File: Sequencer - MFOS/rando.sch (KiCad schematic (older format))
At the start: 0 parts

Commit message: finished sequencer schematic
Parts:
- added 10k1, 4M7: R_US, symbol Device:R_US
- added C15, C20: 0.01u, symbol Device:C
- added C16, C17: 10u, symbol Device:CP1
- added C18, C19: 0.1u, symbol Device:C
- added C21: 0.001u, symbol Device:C
- added C24: 100p, symbol Device:C
- added D48: D, symbol Device:D
- added J73: +12V_Conn, symbol Connector:Conn_01x02_Female
- added J74: GND_Conn, symbol Connector:Conn_01x02_Female
- added J75: -12V_Conn, symbol Connector:Conn_01x02_Female
- added Q1: 2N3904, Package_TO_SOT_THT:TO-92_Inline, symbol Transistor_BJT:2N3904
- added R30, R31: 2M, symbol Device:R_US
- added R32, R35: 4k7, symbol Device:R_US
- added R33: 100K, symbol Device:R_US
- added R34, R36: 1M, symbol Device:R_US
- added U12: CD4094, symbol modular_synth:CD4094
- added U6: 40106, symbol 4xxx:40106
- added U8: TL082, symbol Amplifier_Operational:TL082
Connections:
- new net: C15.2, Q1.1 (E), R31.2
- new net: C15.1, R30.1, U8.3 (+)
- new net: 4M7.1, R33.2, R34.2, U8.1
- new net: 4M7.2, R32.1, U8.2 (-)
- new net: R33.1, U8.5 (+)
- new net: C20.2, R34.1, U8.6 (-)
- new net: D48.2 (A), U8.7
- new net: D48.1 (K), R35.1, U6.1
- new net: U12.2 (DATA), U6.2
- new net: C21.2, R36.2, U6.3
- new net: R36.1, U12.3 (CLK), U6.4
- new net: C24.1, U6.12
- new net: 10k1.1, C24.2, U12.1 (STB)
- new net +12V: C16.1, C18.1, C19.1, J73.1 (Pin_1), J73.2 (Pin_2), R31.1, U12.15 (ENA), U12.16 (VDD), U6.14 (VDD), U8.8 (V+)
- new net -12V: C17.2, J75.1 (Pin_1), J75.2 (Pin_2), Q1.2 (B), U8.4 (V-)
- new net CLK: U6.13
- new net DA: U12.4 (Q1)
- new net DB: U12.5 (Q2)
- new net DC: U12.6 (Q3)
- new net DD: U12.7 (Q4)
- new net Earth: 10k1.2, C16.2, C17.1, C18.2, C19.2, C20.1, C21.1, J74.1 (Pin_1), J74.2 (Pin_2), R30.2, R32.2, R35.2, U12.8 (VSS), U6.7 (VSS)
- no-connect marks 0 -> 7

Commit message: checked over sequencer schematic
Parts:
- R?: renamed from 10k1; value R_US -> 10K
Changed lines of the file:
@@
 $EndComp
 $Comp
-L Device:R_US 10k1
+L Device:R_US R?
 U 1 1 609B0E8A
 P 6150 3050
-F 0 "10k1" H 6218 3096 50  0000 L CNN
-F 1 "R_US" H 6218 3005 50  0000 L CNN
+F 0 "R?" H 6218 3096 50  0000 L CNN
+F 1 "10K" H 6218 3005 50  0000 L CNN
 F 2 "" V 6190 3040 50  0001 C CNN
 F 3 "~" H 6150 3050 50  0001 C CNN

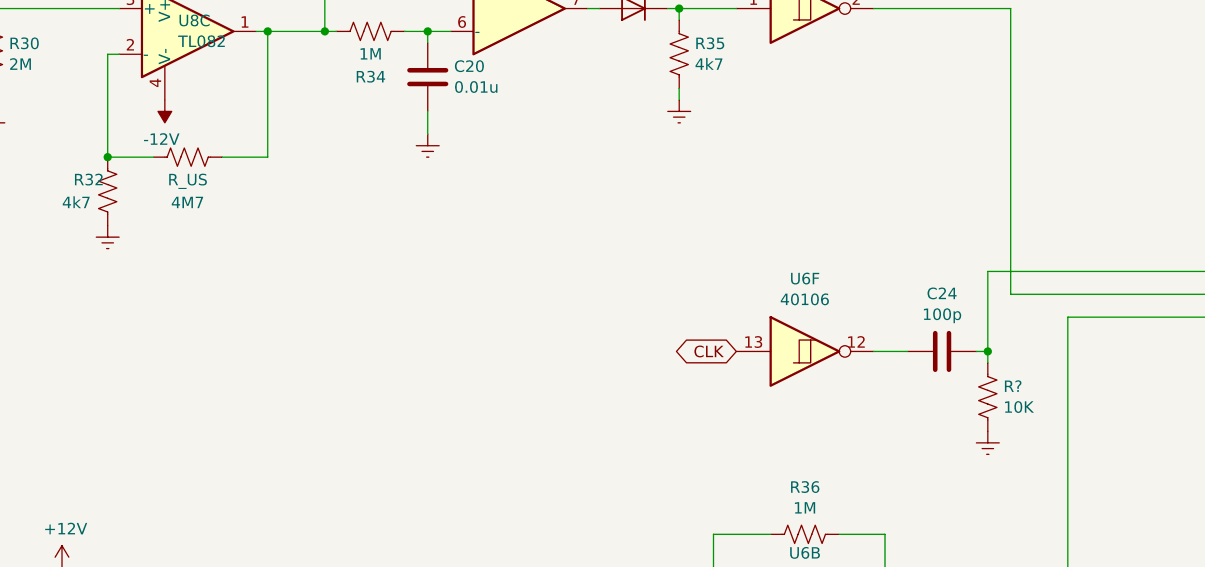
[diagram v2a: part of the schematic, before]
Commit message: sequencer pcb designed and base silkscreen
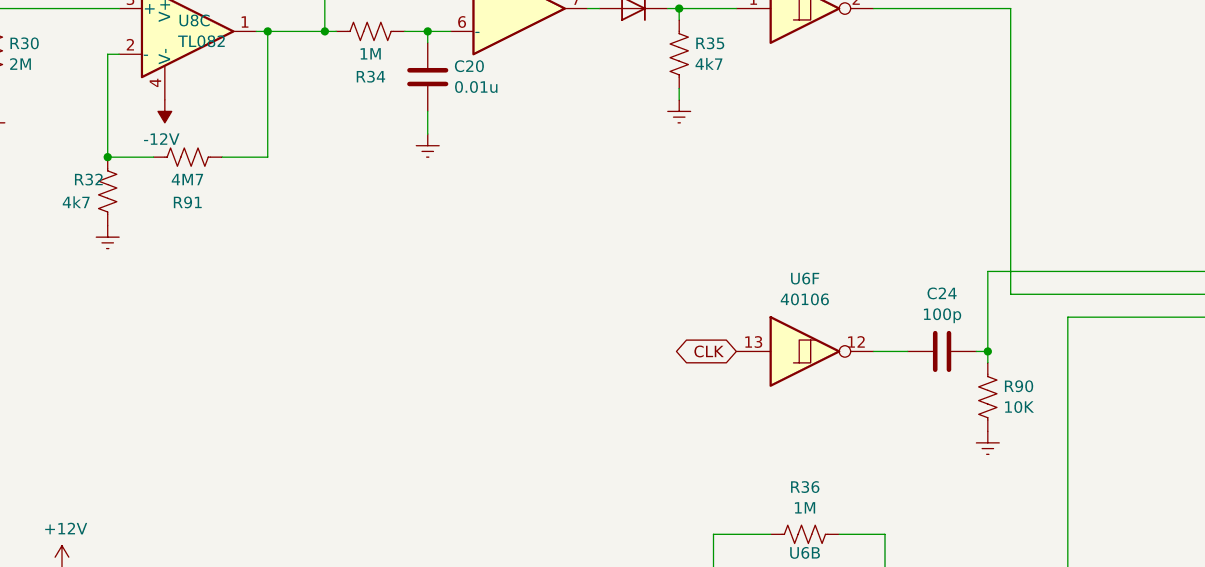
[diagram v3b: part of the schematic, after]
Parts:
- C15, C16, C17, C18, C19, C20, C21, C24: footprint (none) -> Capacitor_THT:C_Rect_L7.0mm_W2.5mm_P5.00mm
- D48: footprint (none) -> Diode_THT:D_T-1_P5.08mm_Horizontal
- J73, J74, J75: footprint (none) -> Connector_Wire:SolderWirePad_1x02_P3.81mm_Drill1mm
- R30, R31, R32, R33, R34, R35, R36: footprint (none) -> Resistor_THT:R_Axial_DIN0207_L6.3mm_D2.5mm_P7.62mm_Horizontal
- R90: renamed from R?; footprint (none) -> Resistor_THT:R_Axial_DIN0207_L6.3mm_D2.5mm_P7.62mm_Horizontal
- R91: renamed from 4M7; value R_US -> 4M7; footprint (none) -> Resistor_THT:R_Axial_DIN0207_L6.3mm_D2.5mm_P7.62mm_Horizontal
- U12: footprint (none) -> Package_DIP:DIP-16_W7.62mm_Socket
- U6: footprint (none) -> Package_DIP:DIP-14_W7.62mm_Socket
- U8: footprint (none) -> Package_DIP:DIP-8_W7.62mm_Socket
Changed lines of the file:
@@
 F 0 "R31" H 1318 1196 50  0000 L CNN
 F 1 "2M" H 1318 1105 50  0000 L CNN
-F 2 "" V 1290 1140 50  0001 C CNN
+F 2 "Resistor_THT:R_Axial_DIN0207_L6.3mm_D2.5mm_P7.62mm_Horizontal" V 1290 1140 50  0001 C CNN
 F 3 "~" H 1250 1150 50  0001 C CNN
 	1    1250 1150
@@
 F 0 "C15" V 1348 1350 50  0000 C CNN
 F 1 "0.01u" V 1439 1350 50  0000 C CNN
-F 2 "" H 1638 1200 50  0001 C CNN
+F 2 "Capacitor_THT:C_Rect_L7.0mm_W2.5mm_P5.00mm" H 1638 1200 50  0001 C CNN
 F 3 "~" H 1600 1350 50  0001 C CNN
 	1    1600 1350
@@
 F 0 "R30" H 1868 1596 50  0000 L CNN
 F 1 "2M" H 1868 1505 50  0000 L CNN
-F 2 "" V 1840 1540 50  0001 C CNN
+F 2 "Resistor_THT:R_Axial_DIN0207_L6.3mm_D2.5mm_P7.62mm_Horizontal" V 1840 1540 50  0001 C CNN
 F 3 "~" H 1800 1550 50  0001 C CNN
 	1    1800 1550
@@
 F 0 "U8" H 2650 1817 50  0000 C CNN
 F 1 "TL082" H 2650 1726 50  0000 C CNN
-F 2 "" H 2650 1450 50  0001 C CNN
+F 2 "Package_DIP:DIP-8_W7.62mm_Socket" H 2650 1450 50  0001 C CNN
 F 3 "http://www.ti.com/lit/ds/symlink/tl081.pdf" H 2650 1450 50  0001 C CNN
 	1    2650 1450
@@
 F 0 "U8" H 4100 1717 50  0000 C CNN
 F 1 "TL082" H 4100 1626 50  0000 C CNN
-F 2 "" H 4100 1350 50  0001 C CNN
+F 2 "Package_DIP:DIP-8_W7.62mm_Socket" H 4100 1350 50  0001 C CNN
 F 3 "http://www.ti.com/lit/ds/symlink/tl081.pdf" H 4100 1350 50  0001 C CNN
 	2    4100 1350
@@
 F 0 "U8" H 2608 1496 50  0000 L CNN
 F 1 "TL082" H 2608 1405 50  0000 L CNN
-F 2 "" H 2650 1450 50  0001 C CNN
+F 2 "Package_DIP:DIP-8_W7.62mm_Socket" H 2650 1450 50  0001 C CNN
 F 3 "http://www.ti.com/lit/ds/symlink/tl081.pdf" H 2650 1450 50  0001 C CNN
 	3    2650 1450
@@
 F 0 "R33" V 3245 1250 50  0000 C CNN
 F 1 "100K" V 3336 1250 50  0000 C CNN
-F 2 "" V 3490 1240 50  0001 C CNN
+F 2 "Resistor_THT:R_Axial_DIN0207_L6.3mm_D2.5mm_P7.62mm_Horizontal" V 3490 1240 50  0001 C CNN
 F 3 "~" H 3450 1250 50  0001 C CNN
 	1    3450 1250
@@
 F 0 "R34" V 3650 1450 50  0000 C CNN
 F 1 "1M" V 3550 1450 50  0000 C CNN
-F 2 "" V 3490 1440 50  0001 C CNN
+F 2 "Resistor_THT:R_Axial_DIN0207_L6.3mm_D2.5mm_P7.62mm_Horizontal" V 3490 1440 50  0001 C CNN
 F 3 "~" H 3450 1450 50  0001 C CNN
 	1    3450 1450
@@
 F 0 "C20" H 3585 1604 50  0000 R CNN
 F 1 "0.01u" H 3585 1695 50  0000 R CNN
-F 2 "" H 3738 1500 50  0001 C CNN
+F 2 "Capacitor_THT:C_Rect_L7.0mm_W2.5mm_P5.00mm" H 3738 1500 50  0001 C CNN
 F 3 "~" H 3700 1650 50  0001 C CNN
 	1    3700 1650
@@
 $EndComp
 $Comp
-L Device:R_US 4M7
+L Device:R_US R91
 U 1 1 609A2A14
 P 2650 2000
-F 0 "4M7" V 2850 2000 50  0000 C CNN
-F 1 "R_US" V 2750 2000 50  0000 C CNN
-F 2 "" V 2690 1990 50  0001 C CNN
+F 0 "R91" V 2850 2000 50  0000 C CNN
+F 1 "4M7" V 2750 2000 50  0000 C CNN
+F 2 "Resistor_THT:R_Axial_DIN0207_L6.3mm_D2.5mm_P7.62mm_Horizontal" V 2690 1990 50  0001 C CNN
 F 3 "~" H 2650 2000 50  0001 C CNN
 	1    2650 2000
@@
 F 0 "R32" H 2150 2200 50  0000 L CNN
 F 1 "4k7" H 2100 2100 50  0000 L CNN
-F 2 "" V 2340 2140 50  0001 C CNN
+F 2 "Resistor_THT:R_Axial_DIN0207_L6.3mm_D2.5mm_P7.62mm_Horizontal" V 2340 2140 50  0001 C CNN
 F 3 "~" H 2300 2150 50  0001 C CNN
 	1    2300 2150
@@
 F 0 "D48" H 4600 1134 50  0000 C CNN
 F 1 "D" H 4600 1225 50  0000 C CNN
-F 2 "" H 4600 1350 50  0001 C CNN
+F 2 "Diode_THT:D_T-1_P5.08mm_Horizontal" H 4600 1350 50  0001 C CNN
 F 3 "~" H 4600 1350 50  0001 C CNN
 	1    4600 1350
@@
 F 0 "R35" H 4868 1596 50  0000 L CNN
 F 1 "4k7" H 4868 1505 50  0000 L CNN
-F 2 "" V 4840 1540 50  0001 C CNN
+F 2 "Resistor_THT:R_Axial_DIN0207_L6.3mm_D2.5mm_P7.62mm_Horizontal" V 4840 1540 50  0001 C CNN
 F 3 "~" H 4800 1550 50  0001 C CNN
 	1    4800 1550
@@
 F 0 "U6" H 5350 1667 50  0000 C CNN
 F 1 "40106" H 5350 1576 50  0000 C CNN
-F 2 "" H 5350 1350 50  0001 C CNN
+F 2 "Package_DIP:DIP-14_W7.62mm_Socket" H 5350 1350 50  0001 C CNN
 F 3 "https://assets.nexperia.com/documents/data-sheet/HEF40106B.pdf" H 5350 1350 50  0001 C CNN
 	1    5350 1350
@@
 F 0 "U6" H 1680 4446 50  0000 L CNN
 F 1 "40106" H 1680 4355 50  0000 L CNN
-F 2 "" H 1450 4400 50  0001 C CNN
+F 2 "Package_DIP:DIP-14_W7.62mm_Socket" H 1450 4400 50  0001 C CNN
 F 3 "https://assets.nexperia.com/documents/data-sheet/HEF40106B.pdf" H 1450 4400 50  0001 C CNN
 	7    1450 4400
@@
 F 0 "U6" H 5350 4367 50  0000 C CNN
 F 1 "40106" H 5350 4276 50  0000 C CNN
-F 2 "" H 5350 4050 50  0001 C CNN
+F 2 "Package_DIP:DIP-14_W7.62mm_Socket" H 5350 4050 50  0001 C CNN
 F 3 "https://assets.nexperia.com/documents/data-sheet/HEF40106B.pdf" H 5350 4050 50  0001 C CNN
 	2    5350 4050
@@
 F 0 "U6" H 5350 3167 50  0000 C CNN
 F 1 "40106" H 5350 3076 50  0000 C CNN
-F 2 "" H 5350 2850 50  0001 C CNN
+F 2 "Package_DIP:DIP-14_W7.62mm_Socket" H 5350 2850 50  0001 C CNN
 F 3 "https://assets.nexperia.com/documents/data-sheet/HEF40106B.pdf" H 5350 2850 50  0001 C CNN
 	6    5350 2850
@@
 F 0 "R36" V 5145 3650 50  0000 C CNN
 F 1 "1M" V 5236 3650 50  0000 C CNN
-F 2 "" V 5390 3640 50  0001 C CNN
+F 2 "Resistor_THT:R_Axial_DIN0207_L6.3mm_D2.5mm_P7.62mm_Horizontal" V 5390 3640 50  0001 C CNN
 F 3 "~" H 5350 3650 50  0001 C CNN
 	1    5350 3650
@@
 F 0 "C21" H 4835 4204 50  0000 R CNN
 F 1 "0.001u" H 4835 4295 50  0000 R CNN
-F 2 "" H 4988 4100 50  0001 C CNN
+F 2 "Capacitor_THT:C_Rect_L7.0mm_W2.5mm_P5.00mm" H 4988 4100 50  0001 C CNN
 F 3 "~" H 4950 4250 50  0001 C CNN
 	1    4950 4250
@@
 F 0 "C24" V 6202 2850 50  0000 C CNN
 F 1 "100p" V 6111 2850 50  0000 C CNN
-F 2 "" H 5988 2700 50  0001 C CNN
+F 2 "Capacitor_THT:C_Rect_L7.0mm_W2.5mm_P5.00mm" H 5988 2700 50  0001 C CNN
 F 3 "~" H 5950 2850 50  0001 C CNN
 	1    5950 2850
@@
 $EndComp
 $Comp
-L Device:R_US R?
+L Device:R_US R90
 U 1 1 609B0E8A
 P 6150 3050
-F 0 "R?" H 6218 3096 50  0000 L CNN
+F 0 "R90" H 6218 3096 50  0000 L CNN
 F 1 "10K" H 6218 3005 50  0000 L CNN
-F 2 "" V 6190 3040 50  0001 C CNN
+F 2 "Resistor_THT:R_Axial_DIN0207_L6.3mm_D2.5mm_P7.62mm_Horizontal" V 6190 3040 50  0001 C CNN
 F 3 "~" H 6150 3050 50  0001 C CNN
 	1    6150 3050
@@
 F 0 "C16" H 2215 4446 50  0000 L CNN
 F 1 "10u" H 2215 4355 50  0000 L CNN
-F 2 "" H 2100 4400 50  0001 C CNN
+F 2 "Capacitor_THT:C_Rect_L7.0mm_W2.5mm_P5.00mm" H 2100 4400 50  0001 C CNN
 F 3 "~" H 2100 4400 50  0001 C CNN
 	1    2100 4400
@@
 F 0 "C18" H 2615 4446 50  0000 L CNN
 F 1 "0.1u" H 2615 4355 50  0000 L CNN
-F 2 "" H 2538 4250 50  0001 C CNN
+F 2 "Capacitor_THT:C_Rect_L7.0mm_W2.5mm_P5.00mm" H 2538 4250 50  0001 C CNN
 F 3 "~" H 2500 4400 50  0001 C CNN
 	1    2500 4400
@@
 F 0 "C19" H 2965 4446 50  0000 L CNN
 F 1 "0.1u" H 2965 4355 50  0000 L CNN
-F 2 "" H 2888 4250 50  0001 C CNN
+F 2 "Capacitor_THT:C_Rect_L7.0mm_W2.5mm_P5.00mm" H 2888 4250 50  0001 C CNN
 F 3 "~" H 2850 4400 50  0001 C CNN
 	1    2850 4400
@@
 F 0 "C17" H 2215 5396 50  0000 L CNN
 F 1 "10u" H 2215 5305 50  0000 L CNN
-F 2 "" H 2100 5350 50  0001 C CNN
+F 2 "Capacitor_THT:C_Rect_L7.0mm_W2.5mm_P5.00mm" H 2100 5350 50  0001 C CNN
 F 3 "~" H 2100 5350 50  0001 C CNN
 	1    2100 5350
@@
 F 0 "U12" H 7800 2900 50  0000 C CNN
 F 1 "CD4094" H 7800 2800 50  0000 C CNN
-F 2 "" H 7800 2850 50  0001 C CNN
+F 2 "Package_DIP:DIP-16_W7.62mm_Socket" H 7800 2850 50  0001 C CNN
 F 3 "" H 7800 2850 50  0001 C CNN
 	1    7800 2850
@@
 F 0 "J73" V 1438 3512 50  0000 R CNN
 F 1 "+12V_Conn" V 1350 3550 50  0000 R CNN
-F 2 "" H 1500 3700 50  0001 C CNN
+F 2 "Connector_Wire:SolderWirePad_1x02_P3.81mm_Drill1mm" H 1500 3700 50  0001 C CNN
 F 3 "~" H 1500 3700 50  0001 C CNN
 	1    1500 3700
@@
 F 0 "J74" V 1446 5148 50  0000 L CNN
 F 1 "GND_Conn" V 1537 5148 50  0000 L CNN
-F 2 "" H 1600 5100 50  0001 C CNN
+F 2 "Connector_Wire:SolderWirePad_1x02_P3.81mm_Drill1mm" H 1600 5100 50  0001 C CNN
 F 3 "~" H 1600 5100 50  0001 C CNN
 	1    1600 5100
@@
 F 0 "J75" H 2000 5550 50  0000 C CNN
 F 1 "-12V_Conn" H 2050 5650 50  0000 C CNN
-F 2 "" H 1900 5850 50  0001 C CNN
+F 2 "Connector_Wire:SolderWirePad_1x02_P3.81mm_Drill1mm" H 1900 5850 50  0001 C CNN
 F 3 "~" H 1900 5850 50  0001 C CNN
 	1    1900 5850
